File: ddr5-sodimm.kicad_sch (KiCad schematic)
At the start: 3 parts, among them J4001 BUS_DDR5_SODIMM_AMPHENOL_1016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

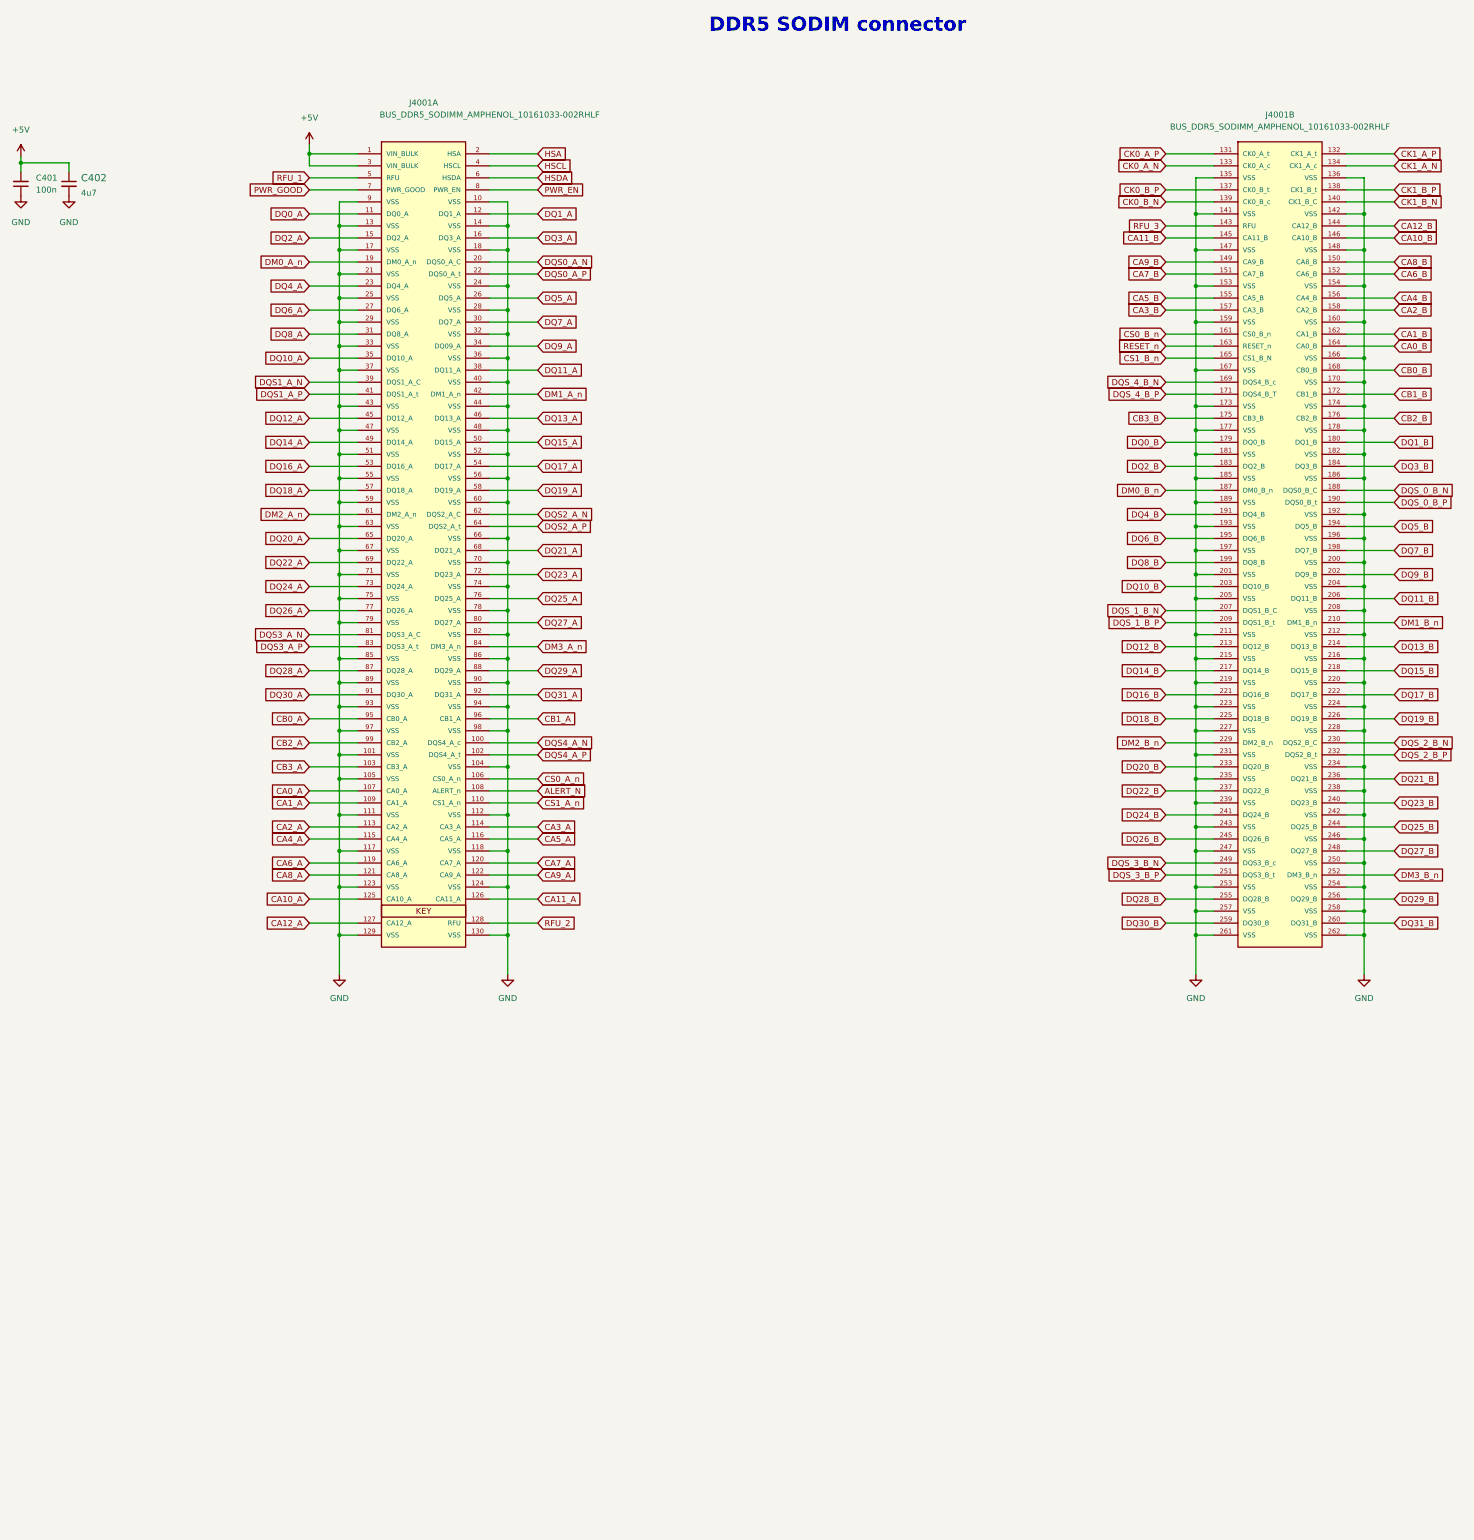
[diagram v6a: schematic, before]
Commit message: Connect control and misc. signals, fix PCIe directions, rework I2C architecture, optimize DC-DC supply utilization
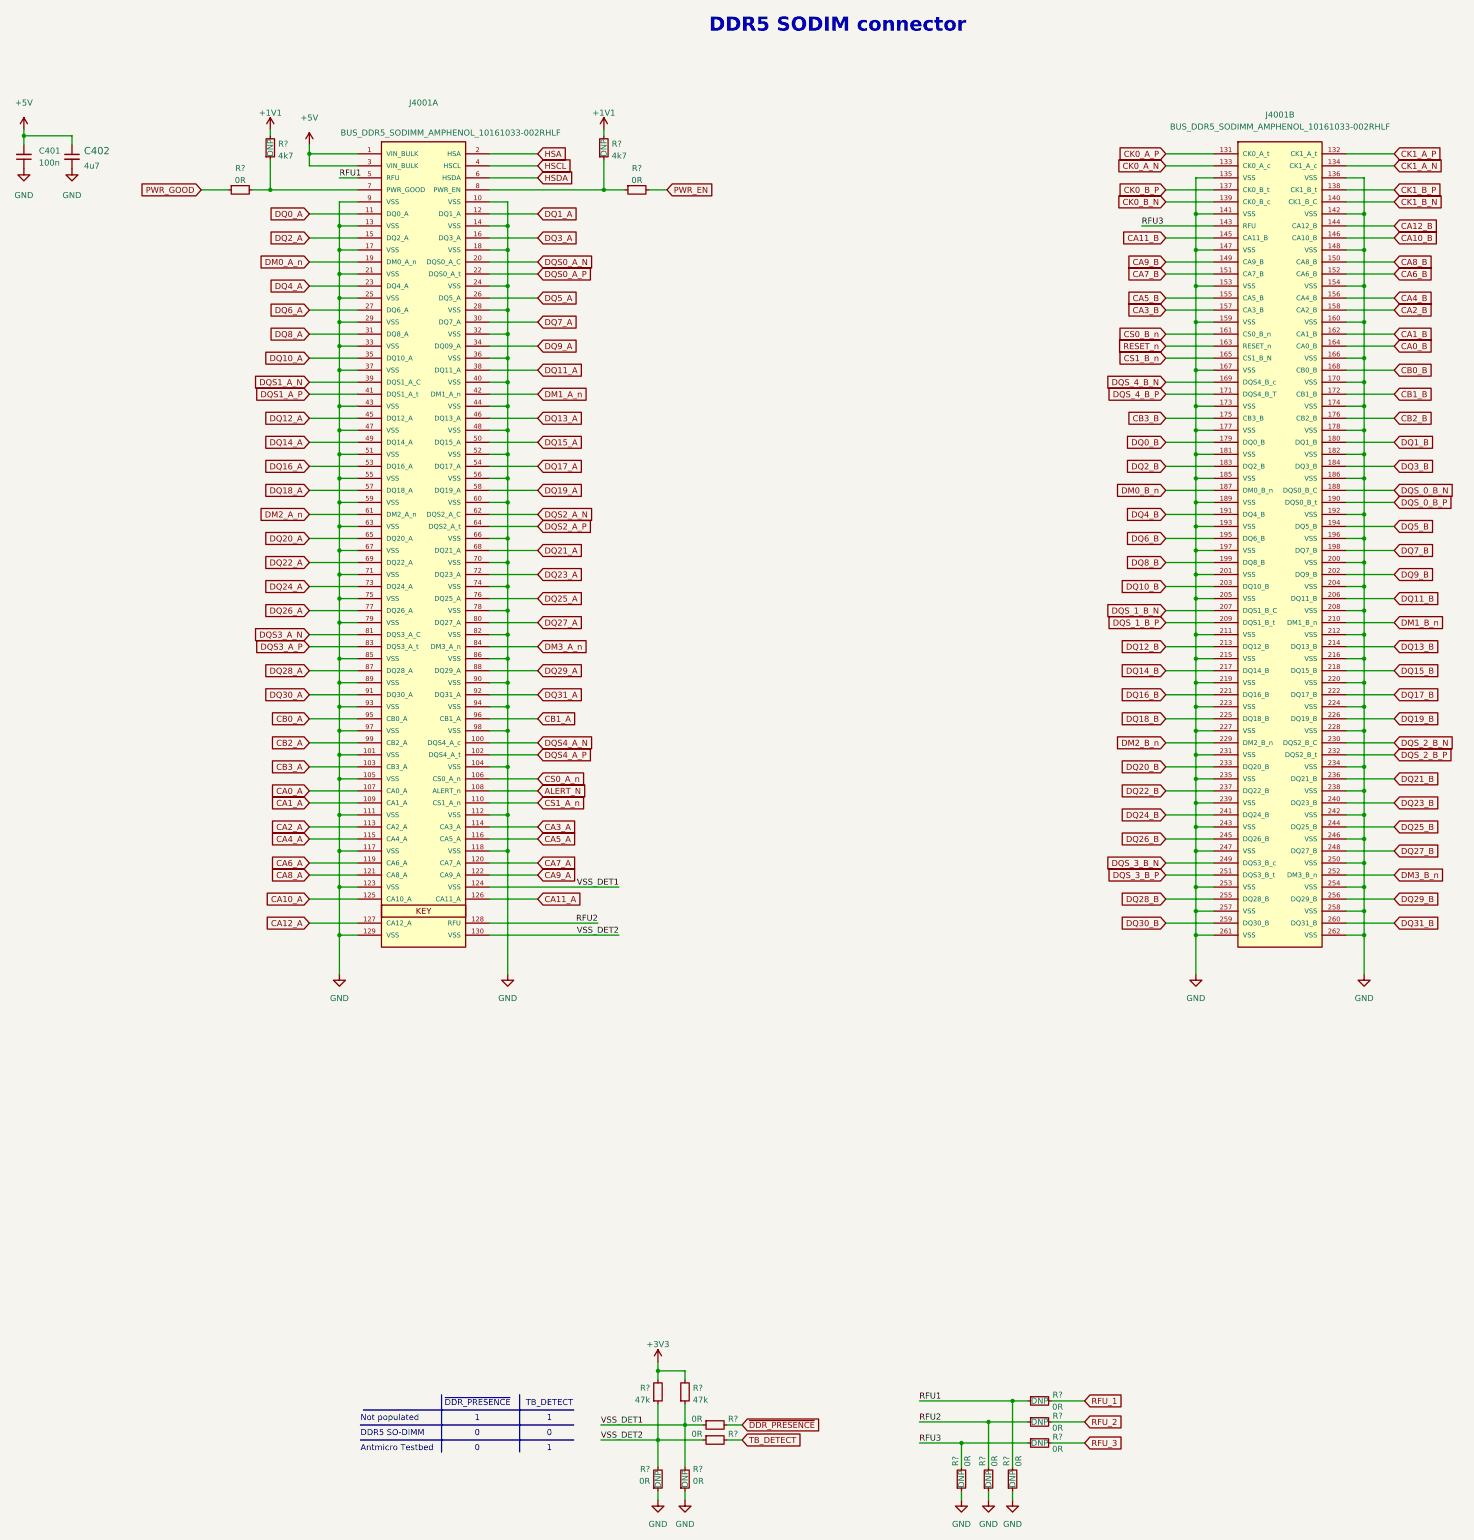
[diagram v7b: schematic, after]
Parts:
- added R? (x12): R_0R_0402, antmicro-footprints:R_0402_1005Metric, symbol antmicroResistors0402:R_0R_0402
- added R? (x2): R_47k_0402, antmicro-footprints:R_0402_1005Metric, symbol antmicroResistors0402:R_47k_0402
- added R? (x2): R_4k7_0402, antmicro-footprints:R_0402_1005Metric, symbol antmicroResistors0402:R_4k7_0402
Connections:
- net GND: now also R?.1, R?.1, R?.1, R?.1, R?.1; no longer J4001.124 (VSS), J4001.130 (VSS)
- net PWR_EN: now also R?.2; no longer J4001.8 (PWR_EN)
- net PWR_GOOD: now also R?.1; no longer J4001.7 (PWR_GOOD)
- net RFU_1: now also R?.2; no longer J4001.5 (RFU)
- net RFU_2: now also R?.2; no longer J4001.128 (RFU)
- net RFU_3: now also R?.2; no longer J4001.143 (RFU)
- new net: J4001.8 (PWR_EN), R?.1, R?.1
- new net: J4001.7 (PWR_GOOD), R?.1, R?.2
- new net +1V1: R?.2, R?.2
- new net +3V3: R?.2, R?.2
- new net RFU1: J4001.5 (RFU), R?.1, R?.2
- new net RFU2: J4001.128 (RFU), R?.1, R?.2
- new net RFU3: J4001.143 (RFU), R?.1, R?.2
- new net TB_DETECT: R?.2
- new net VSS_DET1: J4001.124 (VSS), R?.1, R?.1, R?.2
- new net VSS_DET2: J4001.130 (VSS), R?.1, R?.1, R?.2
- new net ~{DDR_PRESENCE}: R?.2
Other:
- note added: "0"
- note added: "1"
- note added: "Antmicro Testbed"
- note added: "DDR5 SO-DIMM"
- note added: "Not populated"
- note added: "TB_DETECT"
- note added: "~{DDR_PRESENCE}"
- moved on the sheet: C401, C402

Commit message: Sync new components with PCB
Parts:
- gave numbers to parts that had none: 16
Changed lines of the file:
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@@
   (symbol (lib_id "antmicroResistors0402:R_0R_0402") (at 172.72 320.04 0) (unit 1)
     (in_bom yes) (on_board yes)
-    (property "Reference" "R?" (id 0) (at 179.07 318.77 0)
+    (property "Reference" "R4009" (id 0) (at 179.07 318.77 0)
       (effects (font (size 1.27 1.27) (thickness 0.15)))
     )
@@
   (symbol (lib_id "antmicroResistors0402:R_47k_0402") (at 168.91 315.595 90) (unit 1)
     (in_bom yes) (on_board yes) (fields_autoplaced)
-    (property "Reference" "R?" (id 0) (at 170.561 312.2244 90)
+    (property "Reference" "R4007" (id 0) (at 170.561 312.2244 90)
       (effects (font (size 1.27 1.27) (thickness 0.15)) (justify right))
     )
@@
   (symbol (lib_id "sodimm-ddr5-tester:GND") (at 168.91 335.915 0) (unit 1)
     (in_bom yes) (on_board yes) (fields_autoplaced)
-    (property "Reference" "#PWR?" (id 0) (at 168.91 342.265 0)
+    (property "Reference" "#PWR0244" (id 0) (at 168.91 342.265 0)
       (effects (font (size 1.27 1.27)) hide)
     )
@@
   (symbol (lib_id "antmicroResistors0402:R_0R_0402") (at 156.21 59.055 0) (unit 1)
     (in_bom yes) (on_board yes) (fields_autoplaced)
-    (property "Reference" "R?" (id 0) (at 158.75 54.481 0)
+    (property "Reference" "R4004" (id 0) (at 158.75 54.481 0)
       (effects (font (size 1.27 1.27) (thickness 0.15)))
     )
@@
   (symbol (lib_id "antmicroResistors0402:R_0R_0402") (at 163.195 334.01 90) (unit 1)
     (in_bom yes) (on_board yes)
-    (property "Reference" "R?" (id 0) (at 161.5441 329.3735 90)
+    (property "Reference" "R4006" (id 0) (at 161.5441 329.3735 90)
       (effects (font (size 1.27 1.27) (thickness 0.15)) (justify left))
     )
@@
   (symbol (lib_id "sodimm-ddr5-tester:GND") (at 233.045 335.915 0) (unit 1)
     (in_bom yes) (on_board yes) (fields_autoplaced)
-    (property "Reference" "#PWR?" (id 0) (at 233.045 342.265 0)
+    (property "Reference" "#PWR0156" (id 0) (at 233.045 342.265 0)
       (effects (font (size 1.27 1.27)) hide)
     )
@@
   (symbol (lib_id "antmicroResistors0402:R_0R_0402") (at 227.33 334.01 90) (unit 1)
     (in_bom yes) (on_board yes)
-    (property "Reference" "R?" (id 0) (at 226.06 327.66 0)
+    (property "Reference" "R4011" (id 0) (at 226.06 327.66 0)
       (effects (font (size 1.27 1.27) (thickness 0.15)))
     )
@@
   (symbol (lib_id "antmicroResistors0402:R_0R_0402") (at 168.91 334.01 90) (unit 1)
     (in_bom yes) (on_board yes)
-    (property "Reference" "R?" (id 0) (at 170.561 329.3735 90)
+    (property "Reference" "R4008" (id 0) (at 170.561 329.3735 90)
       (effects (font (size 1.27 1.27) (thickness 0.15)) (justify right))
     )
@@
   (symbol (lib_id "antmicroResistors0402:R_47k_0402") (at 163.195 315.595 90) (unit 1)
     (in_bom yes) (on_board yes) (fields_autoplaced)
-    (property "Reference" "R?" (id 0) (at 161.5441 312.2244 90)
+    (property "Reference" "R4005" (id 0) (at 161.5441 312.2244 90)
       (effects (font (size 1.27 1.27) (thickness 0.15)) (justify left))
     )
@@
   (symbol (lib_id "antmicroResistors0402:R_0R_0402") (at 241.3 323.85 0) (unit 1)
     (in_bom yes) (on_board yes)
-    (property "Reference" "R?" (id 0) (at 247.65 322.58 0)
+    (property "Reference" "R4016" (id 0) (at 247.65 322.58 0)
       (effects (font (size 1.27 1.27) (thickness 0.15)))
     )
@@
   (symbol (lib_id "antmicropower:+3V3") (at 163.195 306.705 0) (unit 1)
     (in_bom yes) (on_board yes) (fields_autoplaced)
-    (property "Reference" "#PWR?" (id 0) (at 178.435 309.245 0)
+    (property "Reference" "#PWR0243" (id 0) (at 178.435 309.245 0)
       (effects (font (size 1.27 1.27) (thickness 0.15)) (justify left bottom) hide)
     )
@@
   (symbol (lib_id "antmicroResistors0402:R_0R_0402") (at 172.72 323.215 0) (unit 1)
     (in_bom yes) (on_board yes)
-    (property "Reference" "R?" (id 0) (at 179.07 321.945 0)
+    (property "Reference" "R4010" (id 0) (at 179.07 321.945 0)
       (effects (font (size 1.27 1.27) (thickness 0.15)))
     )
@@
   (symbol (lib_id "antmicroResistors0402:R_0R_0402") (at 241.3 319.405 0) (unit 1)
     (in_bom yes) (on_board yes)
-    (property "Reference" "R?" (id 0) (at 247.65 318.135 0)
+    (property "Reference" "R4015" (id 0) (at 247.65 318.135 0)
       (effects (font (size 1.27 1.27) (thickness 0.15)))
     )
@@
   (symbol (lib_id "sodimm-ddr5-tester:GND") (at 238.125 335.915 0) (unit 1)
     (in_bom yes) (on_board yes) (fields_autoplaced)
-    (property "Reference" "#PWR?" (id 0) (at 238.125 342.265 0)
+    (property "Reference" "#PWR0242" (id 0) (at 238.125 342.265 0)
       (effects (font (size 1.27 1.27)) hide)
     )
@@
   (symbol (lib_id "sodimm-ddr5-tester:GND") (at 163.195 335.915 0) (unit 1)
     (in_bom yes) (on_board yes) (fields_autoplaced)
-    (property "Reference" "#PWR?" (id 0) (at 163.195 342.265 0)
+    (property "Reference" "#PWR0245" (id 0) (at 163.195 342.265 0)
       (effects (font (size 1.27 1.27)) hide)
     )
@@
   (symbol (lib_id "antmicroResistors0402:R_0R_0402") (at 233.045 334.01 90) (unit 1)
     (in_bom yes) (on_board yes)
-    (property "Reference" "R?" (id 0) (at 231.775 327.66 0)
+    (property "Reference" "R4012" (id 0) (at 231.775 327.66 0)
       (effects (font (size 1.27 1.27) (thickness 0.15)))
     )
@@
   (symbol (lib_id "antmicroResistors0402:R_4k7_0402") (at 151.765 52.705 90) (unit 1)
     (in_bom yes) (on_board yes)
-    (property "Reference" "R?" (id 0) (at 153.416 49.3344 90)
+    (property "Reference" "R4003" (id 0) (at 153.416 49.3344 90)
       (effects (font (size 1.27 1.27) (thickness 0.15)) (justify right))
     )
@@
   (symbol (lib_id "antmicroResistors0402:R_0R_0402") (at 72.39 59.055 0) (unit 1)
     (in_bom yes) (on_board yes) (fields_autoplaced)
-    (property "Reference" "R?" (id 0) (at 74.93 54.481 0)
+    (property "Reference" "R4001" (id 0) (at 74.93 54.481 0)
       (effects (font (size 1.27 1.27) (thickness 0.15)))
     )
@@
   (symbol (lib_id "power:+1V1") (at 81.28 46.355 0) (unit 1)
     (in_bom yes) (on_board yes) (fields_autoplaced)
-    (property "Reference" "#PWR?" (id 0) (at 81.28 50.165 0)
+    (property "Reference" "#PWR0247" (id 0) (at 81.28 50.165 0)
       (effects (font (size 1.27 1.27)) hide)
     )
@@
   (symbol (lib_id "power:+1V1") (at 151.765 46.355 0) (unit 1)
     (in_bom yes) (on_board yes) (fields_autoplaced)
-    (property "Reference" "#PWR?" (id 0) (at 151.765 50.165 0)
+    (property "Reference" "#PWR0246" (id 0) (at 151.765 50.165 0)
       (effects (font (size 1.27 1.27)) hide)
     )
@@
   (symbol (lib_id "antmicroResistors0402:R_4k7_0402") (at 81.28 52.705 90) (unit 1)
     (in_bom yes) (on_board yes)
-    (property "Reference" "R?" (id 0) (at 82.931 49.3344 90)
+    (property "Reference" "R4002" (id 0) (at 82.931 49.3344 90)
       (effects (font (size 1.27 1.27) (thickness 0.15)) (justify right))
     )
@@
   (symbol (lib_id "antmicroResistors0402:R_0R_0402") (at 241.3 314.96 0) (unit 1)
     (in_bom yes) (on_board yes)
-    (property "Reference" "R?" (id 0) (at 247.65 313.69 0)
+    (property "Reference" "R4014" (id 0) (at 247.65 313.69 0)
       (effects (font (size 1.27 1.27) (thickness 0.15)))
     )
@@
   (symbol (lib_id "sodimm-ddr5-tester:GND") (at 227.33 335.915 0) (unit 1)
     (in_bom yes) (on_board yes) (fields_autoplaced)
-    (property "Reference" "#PWR?" (id 0) (at 227.33 342.265 0)
+    (property "Reference" "#PWR0151" (id 0) (at 227.33 342.265 0)
       (effects (font (size 1.27 1.27)) hide)
     )
@@
   (symbol (lib_id "antmicroResistors0402:R_0R_0402") (at 238.125 334.01 90) (unit 1)
     (in_bom yes) (on_board yes)
-    (property "Reference" "R?" (id 0) (at 236.855 327.66 0)
-      (effects (font (size 1.27 1.27) (thickness 0.15)))
-    )
+    (property "Reference" "R4013" (id 0) (at 236.855 327.66 0)
+      (effects (font (size 1.27 1.27) (thickness 0.15)))
+    )
